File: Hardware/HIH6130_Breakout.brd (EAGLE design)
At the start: 17.8 x 15.2 mm, 18 parts, among them U1 HIH6131

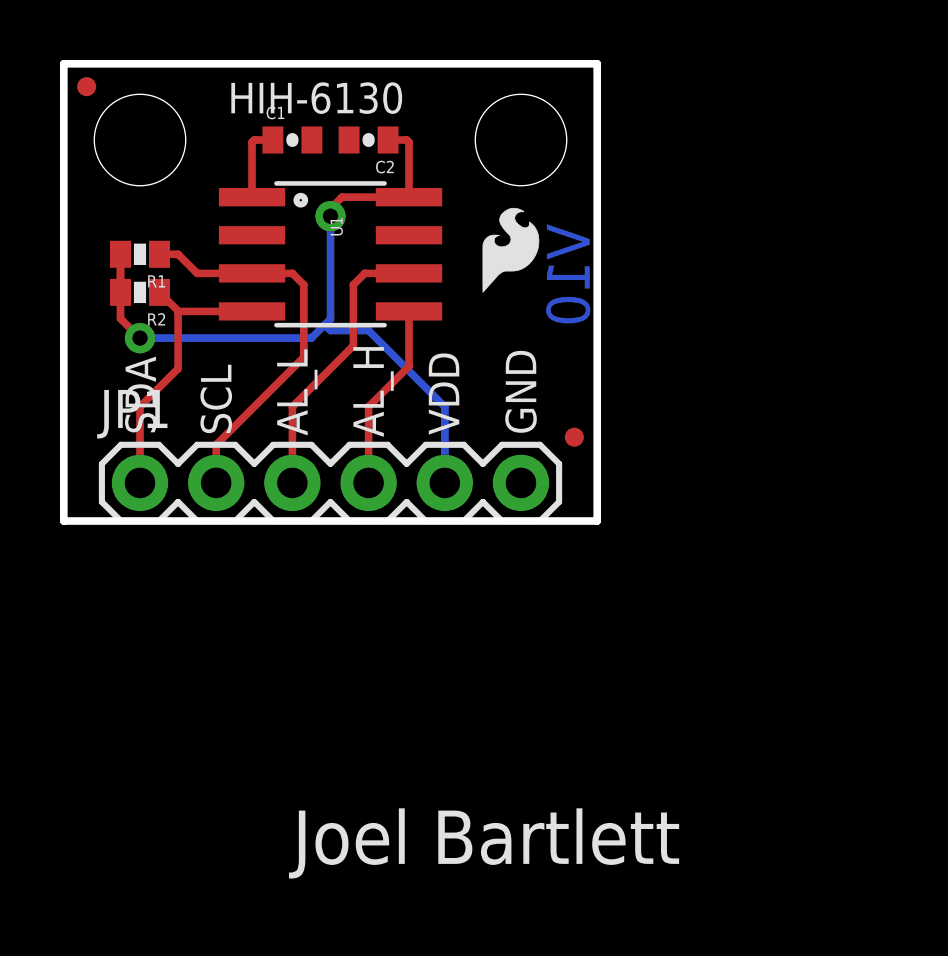
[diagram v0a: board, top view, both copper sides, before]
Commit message: 0402-->0603  Schematic Update
Converted all cap/res to 0603 footprint update schematic to "frame
letter"
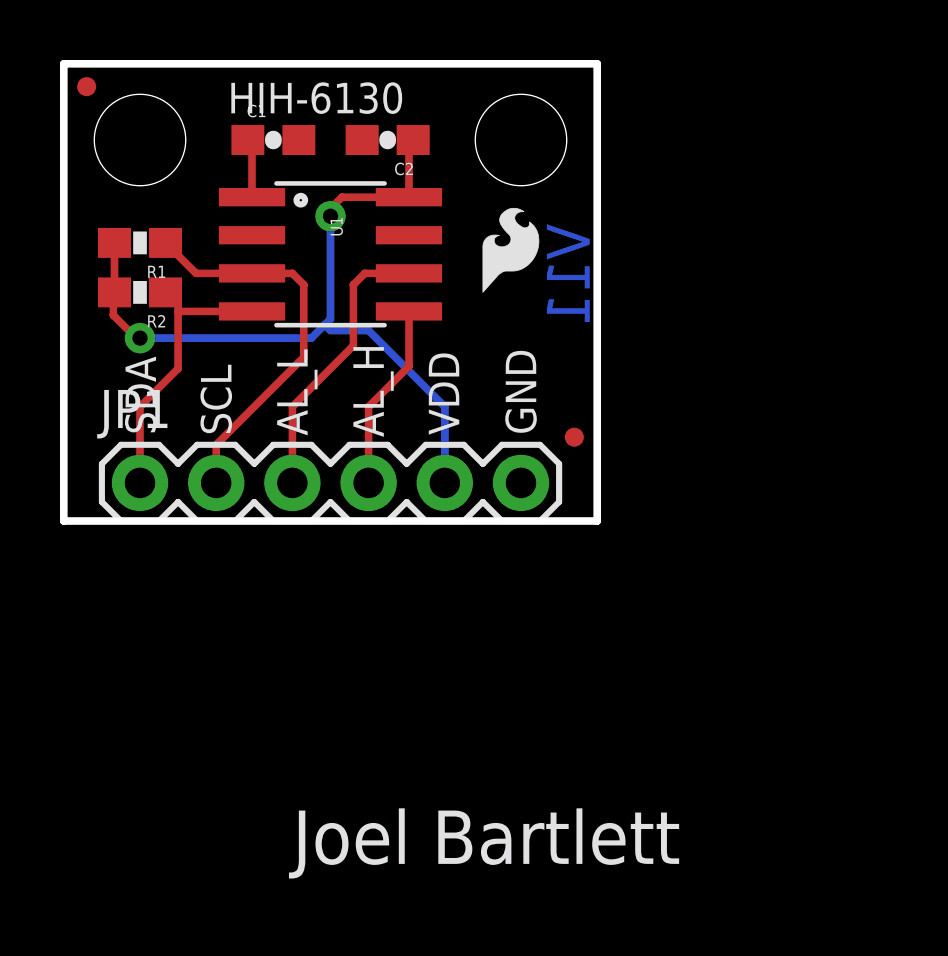
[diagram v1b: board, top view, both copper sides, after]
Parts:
- added FRAME1: FRAME-LETTER, SparkFun-Aesthetics:CREATIVE_COMMONS
- C1, C2: device SparkFun:0402-CAP -> SparkFun-Capacitors:0603-CAP
- R1, R2: device SparkFun:0402-RES -> SparkFun-Resistors:0603-RES
- moved C1 0.63 mm to (6.99, 12.7)
- moved C2 0.63 mm to (10.8, 12.7)
- moved R1 0.38 mm to (2.54, 9.27)
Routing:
- net VCC: track 27.6 -> 26.9 mm
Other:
- board text added: "Revised by: Patrick Alberts"
- board text added: "V11"
- board text removed: "V10"

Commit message: SCH Cleanup
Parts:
- removed U$4: (no value), SparkFun:SFE-LOGO-FLAME
- removed U$5: CREATIVE_COMMONS, SparkFun:CREATIVE_COMMONS
- moved U$2 7.75 mm to (15.2, 8.26), flipped to the top
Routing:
- net SCL: track 13.0 -> 13.7 mm

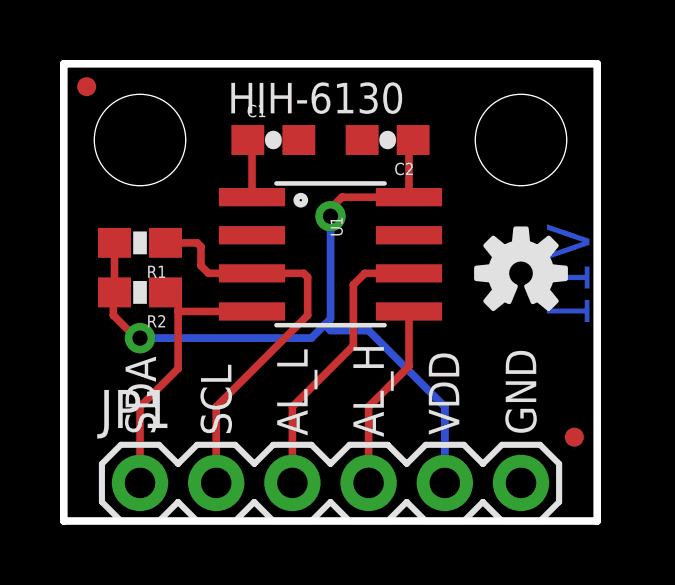
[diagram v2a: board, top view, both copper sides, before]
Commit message: added regular fiducials
also deleted older panel
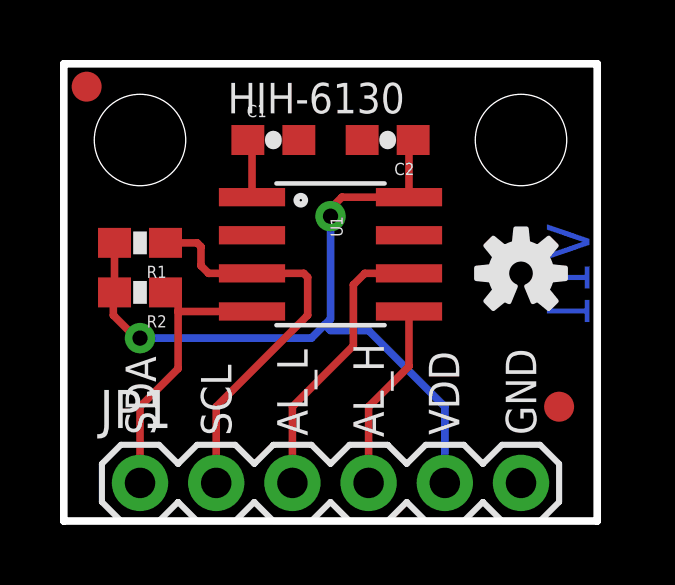
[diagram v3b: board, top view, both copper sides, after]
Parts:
- removed JP2, JP5: FIDUCIALUFIDUCIAL, SparkFun:MICRO-FIDUCIAL
- added FID1, FID2: FIDUCIAL1X2, SparkFun-Aesthetics:FIDUCIAL-1X2
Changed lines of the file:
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@@
 <?xml version="1.0" encoding="utf-8"?>
 <!DOCTYPE eagle SYSTEM "eagle.dtd">
-<eagle version="6.4">
+<eagle version="6.5.0">
 <drawing>
 <settings>
@@
 <setting verticaltext="up"/>
 </settings>
-<grid distance="0.05" unitdist="inch" unit="inch" style="lines" multiple="1" display="yes" altdistance="0.005" altunitdist="inch" altunit="inch"/>
+<grid distance="0.01" unitdist="inch" unit="inch" style="lines" multiple="1" display="yes" altdistance="0.001" altunitdist="inch" altunit="inch"/>
 <layers>
 <layer number="1" name="Top" color="4" fill="1" visible="yes" active="yes"/>
@@
 <layer number="19" name="Unrouted" color="11" fill="1" visible="yes" active="yes"/>
 <layer number="20" name="Dimension" color="6" fill="1" visible="yes" active="yes"/>
-<layer number="21" name="tPlace" color="16" fill="1" visible="yes" active="yes"/>
-<layer number="22" name="bPlace" color="14" fill="1" visible="yes" active="yes"/>
+<layer number="21" name="tPlace" color="6" fill="1" visible="yes" active="yes"/>
+<layer number="22" name="bPlace" color="6" fill="1" visible="yes" active="yes"/>
 <layer number="23" name="tOrigins" color="15" fill="1" visible="yes" active="yes"/>
 <layer number="24" name="bOrigins" color="15" fill="1" visible="yes" active="yes"/>
@@
 <layer number="106" name="bPlate" color="14" fill="3" visible="yes" active="yes"/>
 <layer number="107" name="Crop" color="11" fill="1" visible="yes" active="yes"/>
+<layer number="108" name="tplace-old" color="10" fill="1" visible="yes" active="yes"/>
+<layer number="109" name="ref-old" color="11" fill="1" visible="yes" active="yes"/>
 <layer number="116" name="Patch_BOT" color="9" fill="4" visible="yes" active="yes"/>
 <layer number="121" name="_tsilk" color="7" fill="1" visible="yes" active="yes"/>
@@
 <element name="U$7" library="SparkFun" package="SFE-NEW-WEB-SOLDERMASK" value="" x="15.24" y="6.35" rot="MR0"/>
 <element name="U$8" library="SparkFun" package="SFE-NEW-WEB" value="" x="15.24" y="6.35" rot="MR0"/>
-<element name="JP2" library="SparkFun" package="MICRO-FIDUCIAL" value="FIDUCIALUFIDUCIAL" x="17.018" y="2.794"/>
-<element name="JP5" library="SparkFun" package="MICRO-FIDUCIAL" value="FIDUCIALUFIDUCIAL" x="0.762" y="14.478"/>
 <element name="FRAME1" library="SparkFun-Aesthetics" package="CREATIVE_COMMONS" value="FRAME-LETTER" x="-104.629478125" y="0"/>
+<element name="FID1" library="SparkFun-Aesthetics" package="FIDUCIAL-1X2" value="FIDUCIAL1X2" x="0.762" y="14.478"/>
+<element name="FID2" library="SparkFun-Aesthetics" package="FIDUCIAL-1X2" value="FIDUCIAL1X2" x="16.51" y="3.81"/>
 </elements>
 <signals>
